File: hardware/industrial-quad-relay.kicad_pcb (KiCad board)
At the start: 2 copper layers, 40 x 40 mm, 31 parts, among them P1 CON-SENSOR, P2 Digital Output, P3 Debug, P4 Boot, U1 XMC1XXX24, U2 CPC1020N, U3 CPC1020N, U4 CPC1020N, U5 CPC1020N, U6 DRILL, U7 DRILL, U8 DRILL, U9 DRILL

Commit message: fix headers
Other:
- board text added: "Copyright Tinkerforge GmbH 2018. This documentation describes Open Hardware and is licensed under the CERN OHL v. 1.1. You may redistribute and modify this documentation under the terms of the CERN OHL v.1.1. (http://ohwr.org/cernohl). This documentation is distributed WITHOUT ANY EXPRESS OR IMPLIED WARRANTY, INCLUDING OF MERCHANTABILITY, SATISFACTORY QUALITY AND FITNESS FOR A PARTICULAR PURPOSE.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"
- board text removed: "Copyright Tinkerforge GmbH 2013. This documentation describes Open Hardware and is licensed under the CERN OHL v. 1.1. You may redistribute and modify this documentation under the terms of the CERN OHL v.1.1. (http://ohwr.org/cernohl). This documentation is distributed WITHOUT ANY EXPRESS OR IMPLIED WARRANTY, INCLUDING OF MERCHANTABILITY, SATISFACTORY QUALITY AND FITNESS FOR A PARTICULAR PURPOSE.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"
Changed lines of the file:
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@@
     (links 61)
     (no_connects 0)
-    (area 97.609659 37.858699 137.993121 78.242161)
+    (area 96.944659 37.193699 278.24557 168.441053)
     (thickness 1.6002)
     (drawings 22)
@@
   (title_block
     (title "Industrial Quad Relay Bricklet")
-    (rev 1.1)
+    (date 2018-01-12)
+    (rev 2.0)
     (company "Tinkerforge GmbH")
     (comment 1 "Licensed under CERN OHL v.1.1")
-    (comment 2 "Copyright (©) 2013, B.Nordmeyer <bastian@tinkerforge.com>")
+    (comment 2 "Copyright (©) 2018, B.Nordmeyer <bastian@tinkerforge.com>")
   )
   (layers
@@
   )
   (setup
-    (last_trace_width 0.50038)
+    (last_trace_width 0.14986)
     (user_trace_width 0.14986)
     (user_trace_width 0.29972)
@@
     (effects (font (size 0.70104 0.70104) (thickness 0.14986)))
   )
-  (gr_text "Copyright Tinkerforge GmbH 2013.\nThis documentation describes Open Hardware and is licensed under the\nCERN OHL v. 1.1.\nYou may redistribute and modify this documentation under the terms of the\nCERN OHL v.1.1. (http://ohwr.org/cernohl). This documentation is distributed\nWITHOUT ANY EXPRESS OR IMPLIED WARRANTY, INCLUDING OF\nMERCHANTABILITY, SATISFACTORY QUALITY AND FITNESS FOR A\nPARTICULAR PURPOSE. Please see the CERN OHL v.1.1 for applicable\nconditions" (at 254.29972 162.10026) (layer Cmts.User)
+  (gr_text "Copyright Tinkerforge GmbH 2018.\nThis documentation describes Open Hardware and is licensed under the\nCERN OHL v. 1.1.\nYou may redistribute and modify this documentation under the terms of the\nCERN OHL v.1.1. (http://ohwr.org/cernohl). This documentation is distributed\nWITHOUT ANY EXPRESS OR IMPLIED WARRANTY, INCLUDING OF\nMERCHANTABILITY, SATISFACTORY QUALITY AND FITNESS FOR A\nPARTICULAR PURPOSE. Please see the CERN OHL v.1.1 for applicable\nconditions" (at 253.4 153.85) (layer Cmts.User)
     (effects (font (size 0.8001 0.8001) (thickness 0.200025)))
   )

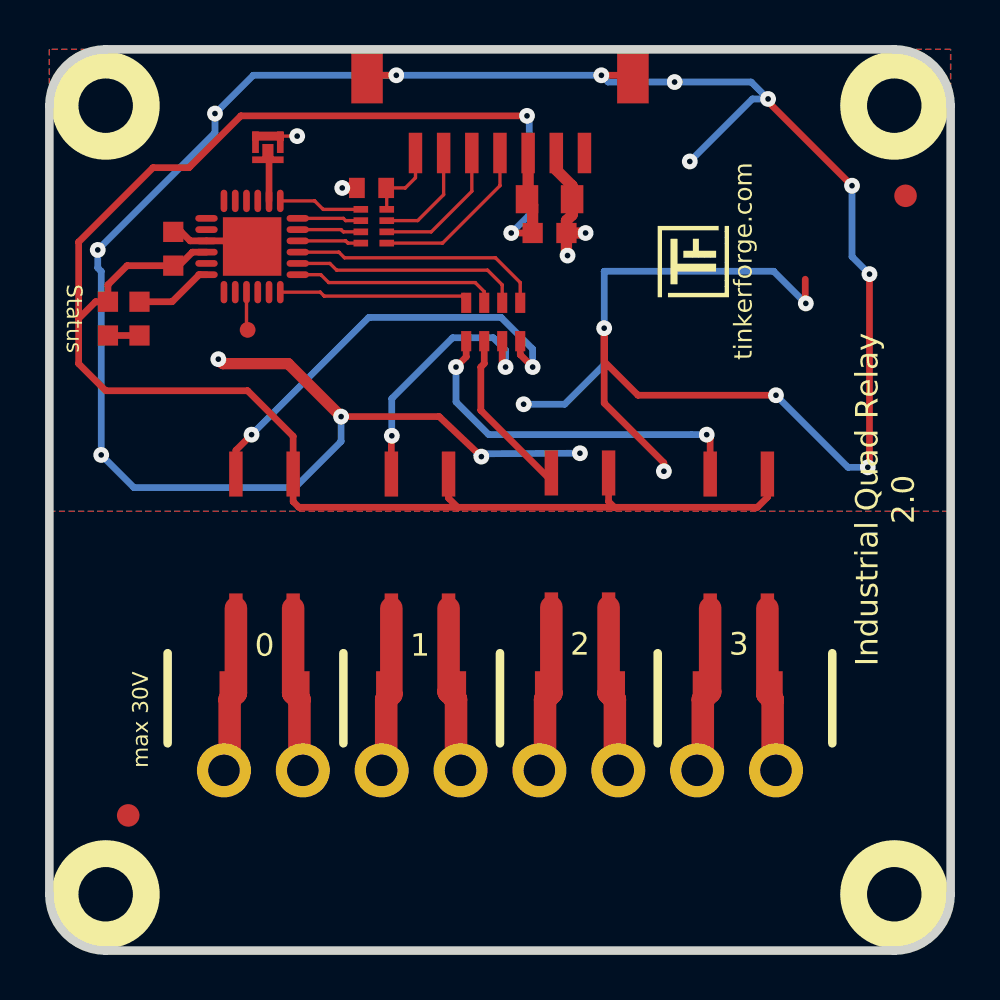
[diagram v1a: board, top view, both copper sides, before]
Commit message: add four status led, routing optimized
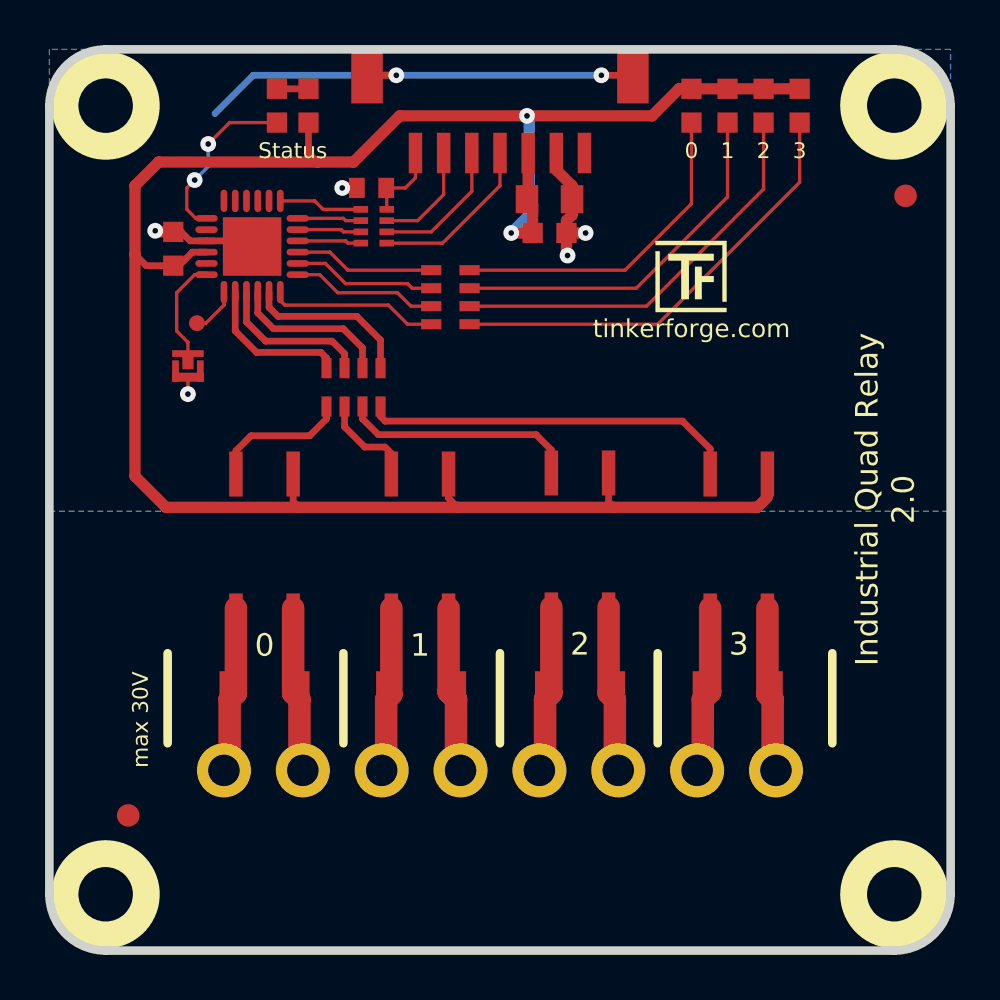
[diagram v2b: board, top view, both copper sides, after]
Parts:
- added D2: blue, D0603F, F.Cu at (126.3, 40.5)
- added D3: blue, D0603F, F.Cu at (127.9, 40.5)
- added D4: blue, D0603F, F.Cu at (129.5, 40.5)
- added D5: blue, D0603F, F.Cu at (131.1, 40.5)
- added RP3: 1k, 0603X4, F.Cu at (115.6, 49.0)
- moved D1 13.0 mm to (109.3, 40.5), turned to 90 degrees
- moved R5 11.2 mm to (107.9, 40.5), turned to 90 degrees
- moved P4 10.3 mm to (104.0, 52.1), turned to 90 degrees
- moved RP1 6.85 mm to (111.3, 53.0)
- moved G*** 2.50 mm to (124.7, 46.5), turned to 0 degrees
- moved P3 2.27 mm to (104.3, 50.2)
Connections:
- RP1 pad 1: OUTPUT1 -> OUTPUT3
- RP1 pad 3: OUTPUT3 -> OUTPUT1
- RP1 pad 4: OUTPUT4 -> OUTPUT0
- U1 pad 12: Net-(R5-Pad1) -> Net-(P4-Pad2)
- U1 pad 13: (no net) -> Net-(P3-Pad1)
- U1 pad 14: (no net) -> OUTPUT0
- U1 pad 15: Net-(P3-Pad1) -> OUTPUT1
- U1 pad 16: (no net) -> OUTPUT2
- U1 pad 17: (no net) -> OUTPUT3
- U1 pad 18: OUTPUT4 -> LED3
- U1 pad 19: OUTPUT3 -> LED2
- U1 pad 2: Net-(P4-Pad2) -> (no net)
- U1 pad 20: OUTPUT2 -> LED1
- U1 pad 21: OUTPUT1 -> LED0
- U1 pad 7: (no net) -> Net-(R5-Pad1)
- U2 pad 2: Net-(RP1-Pad8) -> Net-(RP1-Pad5)
- U3 pad 2: Net-(RP1-Pad7) -> Net-(RP1-Pad6)
- U4 pad 2: Net-(RP1-Pad6) -> Net-(RP1-Pad7)
- U5 pad 2: Net-(RP1-Pad5) -> Net-(RP1-Pad8)
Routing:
- net GND: track 158.2 -> 37.2 mm, vias 24 -> 7
- net Net-(D5-Pad2): track 0.00 -> 19.9 mm
- net Net-(D4-Pad2): track 0.00 -> 18.2 mm
- net Net-(D3-Pad2): track 0.00 -> 16.4 mm
- net Net-(D2-Pad2): track 0.00 -> 14.7 mm
- net Net-(RP1-Pad5): track 16.4 -> 6.19 mm, vias 2 -> 0
- net 3V3: track 84.6 -> 94.6 mm
- net OUTPUT4: track 8.81 -> 0.00 mm
- net LED3: track 0.00 -> 7.51 mm
- net OUTPUT0: track 0.00 -> 6.72 mm
- net LED2: track 0.00 -> 6.50 mm
- net LED1: track 0.00 -> 6.38 mm
- net LED0: track 0.00 -> 6.26 mm
- net OUTPUT1: track 11.3 -> 6.90 mm
- net Net-(R5-Pad1): track 3.47 -> 7.78 mm, vias 0 -> 2
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- removed copper zone on F.Cu, net GND

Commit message: fix logo positions
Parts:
- turned VAL to 90 degrees
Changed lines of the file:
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@@
     (links 73)
     (no_connects 0)
-    (area 97.609659 37.858699 137.993121 78.242161)
+    (area 96.944659 37.193699 277.34585 160.190793)
     (thickness 1.6002)
     (drawings 26)
@@
   (layers
     (0 Front signal)
-    (31 Back signal)
+    (31 Back signal hide)
     (32 B.Adhes user)
     (33 F.Adhes user)
@@
     (aux_axis_origin 97.8 78.05)
     (grid_origin 97.8 78.05)
-    (visible_elements FFFF7FBF)
+    (visible_elements FFFFFFBF)
     (pcbplotparams
       (layerselection 0x00030_80000001)
@@
   )
   (module kicad-libraries:CE_5mm (layer Back)
-    (at 107.8 58.05 270)
-    (fp_text reference VAL (at 0 0 270) (layer B.SilkS) hide
+    (at 107.8 58.05 90)
+    (fp_text reference VAL (at 0 0 90) (layer B.SilkS) hide
       (effects (font (size 0.2 0.2) (thickness 0.05)) (justify mirror))
     )
-    (fp_text value CE_5mm (at 0 0 270) (layer B.SilkS) hide
+    (fp_text value CE_5mm (at 0 0 90) (layer B.SilkS) hide
       (effects (font (size 0.2 0.2) (thickness 0.05)) (justify mirror))
     )
